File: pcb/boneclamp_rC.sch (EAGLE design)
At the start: 160 parts, among them IC1 24C, IC2 LM741D, IC3 LM741D, U1 AD8032ARZ-REEL7, U10 ADA4841-2YRZ, U11 ADA4841-2YRZ, U12 ADS8331IBPW, U13 OPA365AIDBVR, U14 REF5040MDREP, U15 OPA365AIDBVR, U16 OPA365AIDBVR, U2 LT1964ES5-5TRMPBF, U3 OPA365AIDBVR, U4 TLV70245DBVT, U5 ADA4841-2YRZ, U6 AD713JRZ-16, U8 TPS63700DRCT, U9 ADA4841-2YRZ

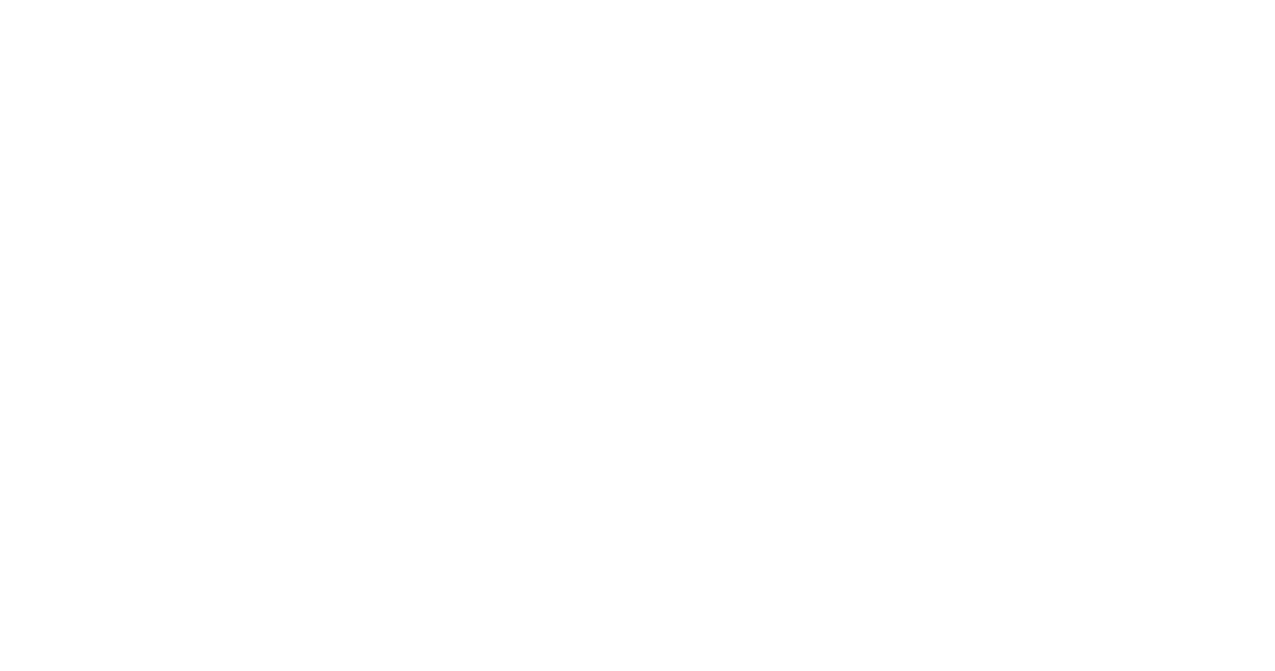
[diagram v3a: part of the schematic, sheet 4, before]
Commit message: Added the switched capacitor voltage inveter, which greatly simiplifies the power supply design.
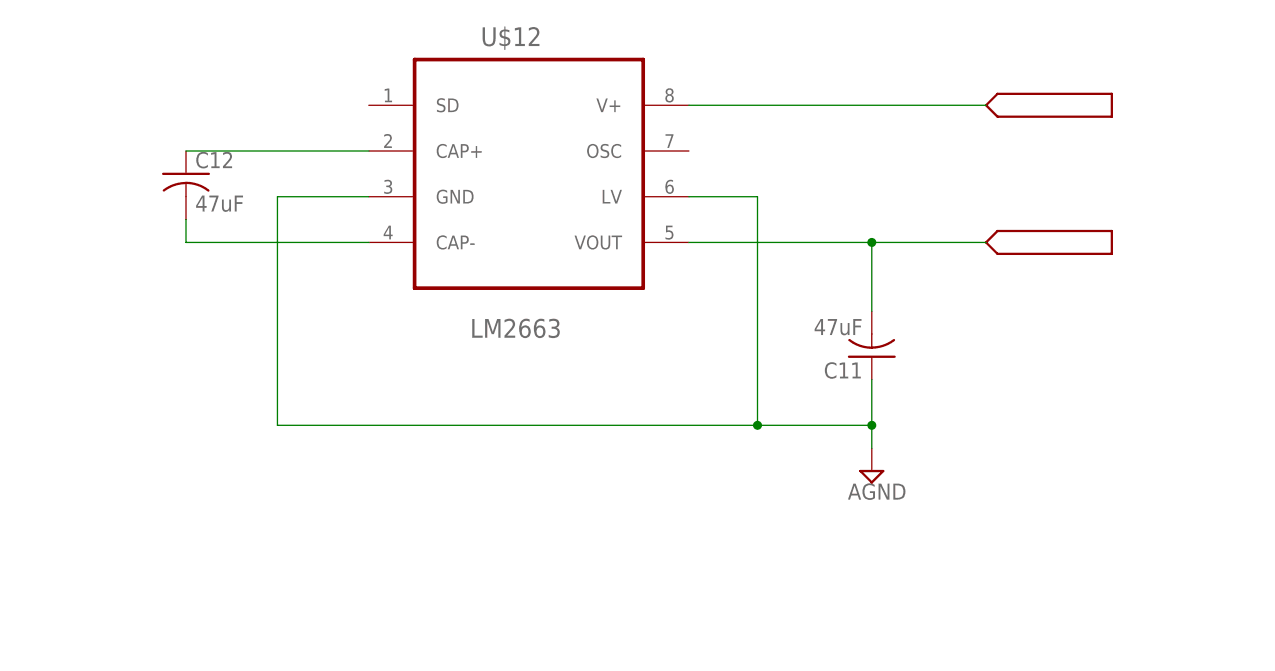
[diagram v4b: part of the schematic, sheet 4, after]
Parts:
- added C11, C12: 47uF, rcl:C-USC1206
- added U$12: LM2663, ti-extended:LM2663
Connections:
- new net N$33: C12.1, U$12.CAP+
- new net N$34: C12.2, U$12.CAP-
- net AGND: now also C11.1, U$12.GND, U$12.LV
- net VDD_5V: now also U$12.V+
- net _VSS: now also C11.2, U$12.VOUT
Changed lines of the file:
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@@
 <part name="R24" library="resistor" deviceset="R-US_" device="R0805" value="1k"/>
 <part name="C3" library="rcl" deviceset="C-EU" device="C0805" value="10uF"/>
+<part name="U$12" library="ti-extended" deviceset="LM2663" device=""/>
+<part name="U$13" library="boneclamp" deviceset="V_SIG" device=""/>
+<part name="C11" library="rcl" deviceset="C-US" device="C1206" value="47uF"/>
+<part name="SUPPLY37" library="supply2" deviceset="AGND" device=""/>
+<part name="U$14" library="boneclamp" deviceset="V_SIG" device=""/>
+<part name="C12" library="rcl" deviceset="C-US" device="C1206" value="47uF"/>
 </parts>
 <sheets>
@@
 <instance part="U$22" gate="G$1" x="-53.34" y="-55.88" rot="R180"/>
 <instance part="U$25" gate="G$1" x="43.18" y="-55.88"/>
+<instance part="U$12" gate="G$1" x="0" y="157.48"/>
+<instance part="U$13" gate="G$1" x="50.8" y="165.1"/>
+<instance part="C11" gate="G$1" x="38.1" y="137.16" rot="R180"/>
+<instance part="SUPPLY37" gate="G$1" x="38.1" y="124.46"/>
+<instance part="U$14" gate="G$1" x="50.8" y="149.86"/>
+<instance part="C12" gate="G$1" x="-38.1" y="157.48"/>
 </instances>
 <busses>
@@
 <junction x="0" y="-83.82"/>
 </segment>
+<segment>
+<pinref part="SUPPLY37" gate="G$1" pin="AGND"/>
+<wire x1="38.1" y1="127" x2="38.1" y2="129.54" width="0.1524" layer="91"/>
+<pinref part="U$12" gate="G$1" pin="LV"/>
+<wire x1="17.78" y1="154.94" x2="25.4" y2="154.94" width="0.1524" layer="91"/>
+<wire x1="25.4" y1="154.94" x2="25.4" y2="129.54" width="0.1524" layer="91"/>
+<wire x1="25.4" y1="129.54" x2="38.1" y2="129.54" width="0.1524" layer="91"/>
+<pinref part="U$12" gate="G$1" pin="GND"/>
+<wire x1="-17.78" y1="154.94" x2="-27.94" y2="154.94" width="0.1524" layer="91"/>
+<wire x1="-27.94" y1="154.94" x2="-27.94" y2="129.54" width="0.1524" layer="91"/>
+<wire x1="-27.94" y1="129.54" x2="25.4" y2="129.54" width="0.1524" layer="91"/>
+<junction x="25.4" y="129.54"/>
+<pinref part="C11" gate="G$1" pin="1"/>
+<wire x1="38.1" y1="129.54" x2="38.1" y2="134.62" width="0.1524" layer="91"/>
+<junction x="38.1" y="129.54"/>
+</segment>
 </net>
 <net name="DGND" class="0">
@@
 <wire x1="-22.86" y1="-60.96" x2="-17.78" y2="-60.96" width="0.1524" layer="91"/>
 <label x="-64.135" y="-56.515" size="1.778" layer="95"/>
+</segment>
+<segment>
+<pinref part="U$12" gate="G$1" pin="V+"/>
+<wire x1="50.8" y1="165.1" x2="17.78" y2="165.1" width="0.1524" layer="91"/>
 </segment>
 </net>
@@
 <label x="-60.96" y="1.905" size="1.778" layer="95"/>
 </segment>
+<segment>
+<pinref part="U$12" gate="G$1" pin="VOUT"/>
+<wire x1="17.78" y1="149.86" x2="38.1" y2="149.86" width="0.1524" layer="91"/>
+<pinref part="C11" gate="G$1" pin="2"/>
+<wire x1="38.1" y1="149.86" x2="50.8" y2="149.86" width="0.1524" layer="91"/>
+<wire x1="38.1" y1="142.24" x2="38.1" y2="149.86" width="0.1524" layer="91"/>
+<junction x="38.1" y="149.86"/>
+</segment>
 </net>
 <net name="N$27" class="0">
@@
 </segment>
 </net>
+<net name="N$34" class="0">
+<segment>
+<pinref part="U$12" gate="G$1" pin="CAP-"/>
+<wire x1="-17.78" y1="149.86" x2="-38.1" y2="149.86" width="0.1524" layer="91"/>
+<wire x1="-38.1" y1="149.86" x2="-38.1" y2="152.4" width="0.1524" layer="91"/>
+<pinref part="C12" gate="G$1" pin="2"/>
+</segment>
+</net>
+<net name="N$33" class="0">
+<segment>
+<pinref part="C12" gate="G$1" pin="1"/>
+<pinref part="U$12" gate="G$1" pin="CAP+"/>
+<wire x1="-38.1" y1="160.02" x2="-17.78" y2="160.02" width="0.1524" layer="91"/>
+</segment>
+</net>

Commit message: Minor changes.
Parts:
- removed C23: 10uF, rcl:C-EUC0603
- removed C24: 22nF, rcl:C-EUC0603
- removed C26: 0.1uF, rcl:C-EUC0603
- removed C27: 4.7nF, rcl:C-EUC0603
- removed C29: 10nF, rcl:C-EUC0603
- removed C30, C31, C32, C33: 4.7uF, rcl:C-EUC0603
- removed C34: 0.22uF, rcl:C-EUC0603
- removed C35: 10pF, rcl:C-EUC0603
- removed D1: SCHOTTKY-DIODE-2, boneclamp:SCHOTTKY-DIODE-2
- removed L1: 4.7uH, boneclamp:L-US
- removed R12: 750, rcl:R-US_R0603
- removed R13: 150k, rcl:R-US_R0603
- removed R5: 100k, rcl:R-US_R0603
- removed U8: TPS63700DRCT, ti-extended:TPS63700DRCT
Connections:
- removed net N$23: C26.1, R5.2, U8.EN, U8.VIN
- removed net N$25: C27.1, U8.COMP
- removed net N$27: D1.A, L1.1, U8.SW
- removed net N$30: C35.1, R12.2, R13.1, U8.FB
- removed net N$31: C34.1, R13.2, U8.VREF
- net AGND: no longer C23.2, C24.2, C26.2, C27.2, C29.2, C30.2, C31.2, C32.2, C33.2, C34.2, L1.2, U8.EP, U8.GND, U8.PS_GND
- net VDD_5V: no longer C23.1, C24.1, R5.1, U8.IN
- net _VSS: no longer C29.1, C30.1, C31.1, C32.1, C33.1, C35.2, D1.C, R12.1, U8.OUT
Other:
- moved on the sheet: C11, C12, U$12

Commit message: Minor changes.
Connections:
- removed net VBIAS: C46.1, U1.-IN2, U1.OUT2
- net VBIAS+: now also C46.1, U1.-IN2, U1.OUT2
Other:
- note added: "Must replace this LDO with something that can accept a +5V supply..."
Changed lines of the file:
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@@
 <description>POWER</description>
 <plain>
+<text x="15.24" y="6.35" size="1.778" layer="97">Must replace this LDO
+with something that can
+accept a +5V supply...</text>
 </plain>
 <instances>
@@
 </segment>
 </net>
-<net name="VBIAS" class="0">
+<net name="VBIAS+" class="0">
 <segment>
 <pinref part="U1" gate="A" pin="-IN2"/>
@@
 <pinref part="R14" gate="G$1" pin="2"/>
 <wire x1="-12.7" y1="-144.78" x2="-33.02" y2="-144.78" width="0.1524" layer="91"/>
-</segment>
-</net>
+<label x="-41.91" y="-145.415" size="1.778" layer="95"/>
+</segment>
+</net>

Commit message: Minor changes.
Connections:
- net AGND: now also U$42.GAIN
- net VDRIVE: no longer U$42.GAIN
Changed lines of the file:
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@@
 <setting verticaltext="up"/>
 </settings>
-<grid distance="0.025" unitdist="inch" unit="inch" style="lines" multiple="1" display="no" altdistance="0.01" altunitdist="inch" altunit="inch"/>
+<grid distance="0.1" unitdist="inch" unit="inch" style="lines" multiple="1" display="no" altdistance="0.01" altunitdist="inch" altunit="inch"/>
 <layers>
 <layer number="1" name="Top" color="4" fill="1" visible="no" active="no"/>
@@
 <pinref part="U$42" gate="G$1" pin="RSTSEL"/>
 <wire x1="-17.78" y1="5.08" x2="-25.4" y2="5.08" width="0.1524" layer="91"/>
-<wire x1="-25.4" y1="5.08" x2="-25.4" y2="-15.24" width="0.1524" layer="91"/>
+<wire x1="-25.4" y1="5.08" x2="-25.4" y2="-5.08" width="0.1524" layer="91"/>
+<pinref part="U$42" gate="G$1" pin="GAIN"/>
+<wire x1="-25.4" y1="-5.08" x2="-25.4" y2="-15.24" width="0.1524" layer="91"/>
+<wire x1="-17.78" y1="-5.08" x2="-25.4" y2="-5.08" width="0.1524" layer="91"/>
+<junction x="-25.4" y="-5.08"/>
 </segment>
 <segment>
@@
 <net name="VDRIVE" class="0">
 <segment>
-<wire x1="-17.78" y1="-10.16" x2="-22.86" y2="-10.16" width="0.1524" layer="91"/>
 <label x="-90.17" y="-8.89" size="1.778" layer="95" rot="R180"/>
 <pinref part="U$42" gate="G$1" pin="VDRIVE"/>
 <pinref part="C4" gate="G$1" pin="1"/>
-<wire x1="-22.86" y1="-10.16" x2="-50.8" y2="-10.16" width="0.1524" layer="91"/>
+<wire x1="-17.78" y1="-10.16" x2="-50.8" y2="-10.16" width="0.1524" layer="91"/>
 <wire x1="-50.8" y1="-10.16" x2="-88.9" y2="-10.16" width="0.1524" layer="91"/>
 <wire x1="-50.8" y1="-15.24" x2="-50.8" y2="-10.16" width="0.1524" layer="91"/>
 <junction x="-50.8" y="-10.16"/>
-<pinref part="U$42" gate="G$1" pin="GAIN"/>
-<wire x1="-17.78" y1="-5.08" x2="-22.86" y2="-5.08" width="0.1524" layer="91"/>
-<wire x1="-22.86" y1="-5.08" x2="-22.86" y2="-10.16" width="0.1524" layer="91"/>
-<junction x="-22.86" y="-10.16"/>
-</segment>
-<segment>
+</segment>
+<segment>

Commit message: Fixed DAC output bias
Biased DAC output, other minor schematic changes
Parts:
- removed D2, D3, D4, D5: 1N4004, diode:1N4004
- removed IC2, IC3: LM741D, linear:LM741D
- removed U11: ADA4841-2YRZ, analog-devices-01:ADA4841-2YRZ
- added C13, C14, C23, C24, C26, C27, C29, C30, C31, C32, C33, C34, C35, C38, C70, C71, C72, C73: (no value), rcl:C-EU102-043X133
- added R12, R13, R5, R52, R53, R54: 33, rcl:R-US_R0603
- added U7, U8: AD8022ARMZ, analog-devices-01:AD8022ARMZ
- C25, C28: value 0.1uF -> (none); device rcl:C-EUC0805 -> rcl:C-EU102-043X133
- R21, R46: value (none) -> 33; device rcl:POTENTIOMETER_PT-10S -> rcl:R-US_R0603
- R22, R34, R35, R45: value 1k -> 33; device resistor:R-US_0204/2V -> rcl:R-US_R0603
- R31, R38, R43, R44: value 0.1k -> 33; device rcl:R-US_R0805 -> rcl:R-US_R0603
- R39, R40, R41, R42: value 10k -> 33; device rcl:R-US_R0805 -> rcl:R-US_R0603
- U10: value ADA4841-2YRZ -> AD8022ARMZ; device analog-devices-01:ADA4841-2YRZ -> analog-devices-01:AD8022ARMZ
- U6: value AD713JRZ-16 -> AD8022ARMZ; device analog-devices-01:AD713JRZ-16 -> analog-devices-01:AD8022ARMZ
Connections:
- removed net .5VREF-: IC2.-IN, R21.1, R34.1, R35.2
- removed net .5VREF-1: C25.1, IC3.-IN, R46.1
- removed net GND: C28.2, IC2.+IN, R45.1, U6.NC, U6.NC_2
- removed net VBIAS_DOWN: D2.C, D3.C, D4.C, D5.C, IC2.OUT, R21.2, U6.-IN, U6.-IN_2, U6.-IN_3, U6.-IN_4
- removed net VBIAS_UP: IC3.OUT, R31.2, R38.2, R39.1, R39.2, R40.1, R40.2, R41.1, R41.2, R42.1, R42.2, R43.2, R44.2, R46.2, U10.-IN1, U10.-IN2, U11.-IN1, U11.-IN2
- new net N$11: C13.2, R41.1, R43.2, U7.OUT1
- new net N$23: C27.2, R22.1, R34.2, U6.OUT1
- new net N$27: R43.1, R45.2, U10.-IN1
- new net N$30: R35.1, R38.1, R41.2, U7.-IN1
- new net N$31: R44.1, R46.2, U10.-IN2
- new net N$39: R39.1, R40.1, R42.2, U7.-IN2
- new net N$45: C34.2, U10.+IN2
- new net N$46: C33.2, U10.+IN1
- new net N$50: R34.1, R53.2, U8.-IN1
- new net N$52: R52.1, R54.2, U8.-IN2
- new net N$53: R13.1, R21.1, R31.2, U6.-IN2
- new net N$54: R12.1, R22.2, R5.1, U6.-IN1
- new net N$57: C70.2, U8.+IN2
- new net N$58: C38.2, U8.+IN1
- new net _DAC_A_BIASED: R53.1, U8.OUT1
- new net _DAC_BIASED_B: R54.1, U8.OUT2
- new net _DAC_C_BIASED: R45.1, U10.OUT1
- new net _DAC_D_BIASED: R46.1, U10.OUT2
- net ADC_A: no longer U10.+IN1
- net ADC_B: no longer U10.+IN2
- net ADC_C: no longer U11.+IN1
- net ADC_D: no longer U11.+IN2
- net AGND: now also C13.1, C14.1, C23.1, C24.1, C25.1, C26.1, C27.1, C28.1, C29.1, C30.1, C31.1, C32.1, C33.1, C34.1, C35.1, C38.1, C70.1, C71.1, C72.1, C73.1, U6.+IN1, U6.+IN2, U7.+IN1, U7.+IN2
- net N$10: now also C14.2, R42.1, R44.2, U7.OUT2; no longer IC3.+IN, R22.1, R45.2
- net N$12: now also C28.2, R31.1, R52.2, U6.OUT2; no longer C28.1, R35.1
- net VBIAS-: now also R21.2, R35.2, R40.2, R5.2
- net VDD: now also C26.2, C32.2, C72.2, C73.2, U7.+VS, U8.+VS; no longer IC2.V+, IC3.V+, U11.+VS
- net VREF: no longer R22.2, R34.2
- net VSS: now also C25.2, C31.2, C35.2, C71.2, U7.-VS, U8.-VS; no longer IC2.V-, IC3.V-, U11.-VS
- net _ADC_A: no longer R38.1, U10.OUT1
- net _ADC_B: no longer R31.1, U10.OUT2
- net _ADC_C: no longer R43.1, U11.OUT1
- net _ADC_D: no longer R44.1, U11.OUT2
- net _DAC_A: now also C29.2, R12.2; no longer D2.A, U6.+IN, U6.OUT
- net _DAC_B: now also C30.2, R13.2; no longer D5.A, U6.+IN_2, U6.OUT_2
- net _DAC_C: now also C23.2, R38.2; no longer D4.A, U6.+IN_3, U6.OUT_3
- net _DAC_D: now also C24.2, R39.2; no longer D3.A, U6.+IN_4, U6.OUT_4
